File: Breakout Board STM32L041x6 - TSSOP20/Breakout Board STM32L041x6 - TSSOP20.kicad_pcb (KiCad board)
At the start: 2 copper layers, 35.6 x 33 mm, 35 parts, among them J1 Conn_01x10, J2 Conn_01x10, SW1 reset switch, SW2 ibm m, U1 STM32L041F6P7, Y1 Crystal 32768

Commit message: Update
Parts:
- removed ? (x4): , 
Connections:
- J1 pad 8: /key -> (no net)
- TP5 pad 1: Net-(TP5-Pad1) -> (no net)
- TP6 pad 1: Net-(TP6-Pad1) -> (no net)
- TP7 pad 1: Net-(TP7-Pad1) -> (no net)
- TP8 pad 1: Net-(TP8-Pad1) -> (no net)
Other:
- rule trace_min: 0.2 -> 0.25

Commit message: Update
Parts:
- added ?: , , F.Cu at (132.1, 76.2)
- added ?: , , F.Cu at (26.0, 0.00)
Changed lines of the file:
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@@
     (tracks 30)
     (zones 0)
-    (modules 31)
+    (modules 33)
     (nets 25)
   )
@@
     (add_net "Net-(R5-Pad2)")
   )
+  (module "" (layer F.Cu)
+    (at 132.08 76.2)
+    (fp_text reference "" (at 26.035 0) (layer F.SilkS)
+      (effects (font (size 1.27 1.27) (thickness 0.15)))
+    )
+    (fp_text value "" (at 26.035 0) (layer F.SilkS)
+      (effects (font (size 1.27 1.27) (thickness 0.15)))
+    )
+    (fp_text user vddext (at 9.525 6.985 -90) (layer B.SilkS)
+      (effects (font (size 0.8 0.8) (thickness 0.15)) (justify mirror))
+    )
+  )
+  (module "" (layer F.Cu)
+    (at 26.035 0)
+    (fp_text reference "" (at 135.995 73.13) (layer F.SilkS)
+      (effects (font (size 1.27 1.27) (thickness 0.15)))
+    )
+    (fp_text value "" (at 135.995 73.13) (layer F.SilkS)
+      (effects (font (size 1.27 1.27) (thickness 0.15)))
+    )
+    (fp_text user gnd (at 115.57 68.58 -90) (layer B.SilkS)
+      (effects (font (size 0.8 0.8) (thickness 0.15)) (justify mirror))
+    )
+    (fp_text user swclk (at 113.665 61.595) (layer B.SilkS)
+      (effects (font (size 0.8 0.8) (thickness 0.15)) (justify mirror))
+    )
+    (fp_text user swdio (at 115.57 65.405 -90) (layer B.SilkS)
+      (effects (font (size 0.8 0.8) (thickness 0.15)) (justify mirror))
+    )
+  )
   (module "Breakout Board STM32L041x6 - TSSOP20:Crystal 32768 Hz Citizen - CMR200T32.768KDZB-UT" (layer B.Cu)
     (at 135.995 73.13 180)
@@
       (effects (font (size 0.8 0.8) (thickness 0.15)))
     )
-    (fp_text value 100nF (at 2.775 0.446) (layer F.SilkS)
+    (fp_text value 100nF (at 2.565 0.446) (layer F.SilkS)
       (effects (font (size 0.8 0.8) (thickness 0.15)))
     )
@@
     (effects (font (size 0.7 0.7) (thickness 0.13)) (justify left mirror))
   )
-  (gr_text x2 (at 145.415 60.96) (layer F.SilkS)
+  (gr_text x2 (at 146.05 59.055) (layer F.SilkS)
     (effects (font (size 0.8 0.8) (thickness 0.15)))
   )
@@
     (effects (font (size 0.8 0.8) (thickness 0.15)) (justify mirror))
   )
-  (gr_text x2 (at 145.415 60.96) (layer B.SilkS)
+  (gr_text x2 (at 146.05 59.055) (layer B.SilkS)
     (effects (font (size 0.8 0.8) (thickness 0.15)) (justify mirror))
   )

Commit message: Update
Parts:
- SW1: value reset switch -> reset
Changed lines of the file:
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@@
       (effects (font (size 0.8 0.8) (thickness 0.15)))
     )
-    (fp_text value "reset switch" (at 4.05 9.85 180) (layer F.SilkS)
+    (fp_text value reset (at 4.05 7.83 180) (layer F.SilkS)
       (effects (font (size 0.8 0.8) (thickness 0.15)))
     )
@@
     (effects (font (size 0.7 0.7) (thickness 0.13)) (justify left mirror))
   )
-  (gr_text x2 (at 146.05 59.055) (layer F.SilkS)
+  (gr_text x2 (at 145.415 59.69) (layer F.SilkS)
     (effects (font (size 0.8 0.8) (thickness 0.15)))
   )
@@
     (effects (font (size 0.8 0.8) (thickness 0.15)) (justify mirror))
   )
-  (gr_text x2 (at 146.05 59.055) (layer B.SilkS)
+  (gr_text x2 (at 145.415 59.69) (layer B.SilkS)
     (effects (font (size 0.8 0.8) (thickness 0.15)) (justify mirror))
   )

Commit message: Update
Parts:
- removed ? (x2): , 
- SW1: value reset -> reset sw
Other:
- board text added: "swdio"
- board text added: "vddext"
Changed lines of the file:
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@@
   (general
     (thickness 1.6)
-    (drawings 92)
+    (drawings 95)
     (tracks 30)
     (zones 0)
-    (modules 33)
+    (modules 31)
     (nets 25)
   )
@@
     (add_net "Net-(R5-Pad2)")
   )
-  (module "" (layer F.Cu)
-    (at 132.08 76.2)
-    (fp_text reference "" (at 26.035 0) (layer F.SilkS)
-      (effects (font (size 1.27 1.27) (thickness 0.15)))
-    )
-    (fp_text value "" (at 26.035 0) (layer F.SilkS)
-      (effects (font (size 1.27 1.27) (thickness 0.15)))
-    )
-    (fp_text user vddext (at 9.525 6.985 -90) (layer B.SilkS)
-      (effects (font (size 0.8 0.8) (thickness 0.15)) (justify mirror))
-    )
-  )
-  (module "" (layer F.Cu)
-    (at 26.035 0)
-    (fp_text reference "" (at 135.995 73.13) (layer F.SilkS)
-      (effects (font (size 1.27 1.27) (thickness 0.15)))
-    )
-    (fp_text value "" (at 135.995 73.13) (layer F.SilkS)
-      (effects (font (size 1.27 1.27) (thickness 0.15)))
-    )
-    (fp_text user gnd (at 115.57 68.58 -90) (layer B.SilkS)
-      (effects (font (size 0.8 0.8) (thickness 0.15)) (justify mirror))
-    )
-    (fp_text user swclk (at 113.665 61.595) (layer B.SilkS)
-      (effects (font (size 0.8 0.8) (thickness 0.15)) (justify mirror))
-    )
-    (fp_text user swdio (at 115.57 65.405 -90) (layer B.SilkS)
-      (effects (font (size 0.8 0.8) (thickness 0.15)) (justify mirror))
-    )
-  )
   (module "Breakout Board STM32L041x6 - TSSOP20:Crystal 32768 Hz Citizen - CMR200T32.768KDZB-UT" (layer B.Cu)
     (at 135.995 73.13 180)
@@
       (effects (font (size 0.8 0.8) (thickness 0.15)))
     )
-    (fp_text value reset (at 4.05 7.83 180) (layer F.SilkS)
+    (fp_text value "reset sw" (at 4.05 8.846 180) (layer F.SilkS)
       (effects (font (size 0.8 0.8) (thickness 0.15)))
     )
@@
     (pad 1 thru_hole circle (at 0 0) (size 1.7 1.7) (drill 1) (layers *.Cu *.Mask))
   )
+  (gr_text vddext (at 141.605 83.185 90) (layer B.SilkS)
+    (effects (font (size 0.8 0.8) (thickness 0.15)) (justify mirror))
+  )
+  (gr_text gnd (at 141.605 68.58 90) (layer B.SilkS)
+    (effects (font (size 0.8 0.8) (thickness 0.15)) (justify mirror))
+  )
+  (gr_text swdio (at 141.605 65.405 90) (layer B.SilkS)
+    (effects (font (size 0.8 0.8) (thickness 0.15)) (justify mirror))
+  )
   (gr_text "ЕС1832\n17072019а0" (at 123.19 62.865 90) (layer F.SilkS)
     (effects (font (size 0.8 0.8) (thickness 0.15)))
@@
   (segment (start 124.42 70.63) (end 128.07 70.63) (width 0.25) (layer B.Cu) (net 2) (status 30))
   (segment (start 131.87 72.13) (end 132.12 71.88) (width 0.25) (layer B.Cu) (net 4) (status 30))
-  (via (at 130.192559 72.123691) (size 0.8) (drill 0.4) (layers F.Cu B.Cu) (net 4))
+  (via (at 130.192559 72.123691) (size 0.8) (drill 0.4) (layers F.Cu B.Cu) (net 4) (status 1000000))
   (segment (start 130.192559 72.632441) (end 130.192559 72.123691) (width 0.25) (layer F.Cu) (net 4))
   (segment (start 129.795 73.03) (end 130.192559 72.632441) (width 0.25) (layer F.Cu) (net 4))

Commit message: Update
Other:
- board text added: "!!! CHECK !!! NO 12.5 pF XTAL ALLOWED"
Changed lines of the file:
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@@
   (general
     (thickness 1.6)
-    (drawings 95)
+    (drawings 96)
     (tracks 30)
     (zones 0)
@@
   (page A4)
   (layers
-    (0 F.Cu signal)
-    (31 B.Cu signal)
+    (0 F.Cu signal hide)
+    (31 B.Cu signal hide)
     (32 B.Adhes user)
     (33 F.Adhes user)
@@
     (solder_mask_min_width 0.25)
     (aux_axis_origin 0 0)
-    (visible_elements 7FFFF7FF)
+    (visible_elements 7FFF77FF)
     (pcbplotparams
       (layerselection 0x010fc_ffffffff)
@@
     (pad 1 thru_hole circle (at 0 0) (size 1.7 1.7) (drill 1) (layers *.Cu *.Mask))
   )
+  (gr_text "!!! CHECK !!!\nNO 12.5 pF\nXTAL ALLOWED" (at 135.89 72.39) (layer B.SilkS)
+    (effects (font (size 0.5 0.5) (thickness 0.1)) (justify mirror))
+  )
   (gr_text vddext (at 141.605 83.185 90) (layer B.SilkS)

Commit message: Update
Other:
- board text added: "swclk"
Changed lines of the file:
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@@
   (general
     (thickness 1.6)
-    (drawings 96)
+    (drawings 97)
     (tracks 30)
     (zones 0)
@@
   (page A4)
   (layers
-    (0 F.Cu signal hide)
-    (31 B.Cu signal hide)
+    (0 F.Cu signal)
+    (31 B.Cu signal)
     (32 B.Adhes user)
     (33 F.Adhes user)
@@
     (solder_mask_min_width 0.25)
     (aux_axis_origin 0 0)
-    (visible_elements 7FFF77FF)
+    (visible_elements 7FFFF7FF)
     (pcbplotparams
       (layerselection 0x010fc_ffffffff)
@@
     (pad 1 thru_hole circle (at 0 0) (size 1.7 1.7) (drill 1) (layers *.Cu *.Mask))
   )
+  (gr_text swclk (at 139.7 61.595) (layer B.SilkS)
+    (effects (font (size 0.8 0.8) (thickness 0.15)))
+  )
   (gr_text "!!! CHECK !!!\nNO 12.5 pF\nXTAL ALLOWED" (at 135.89 72.39) (layer B.SilkS)

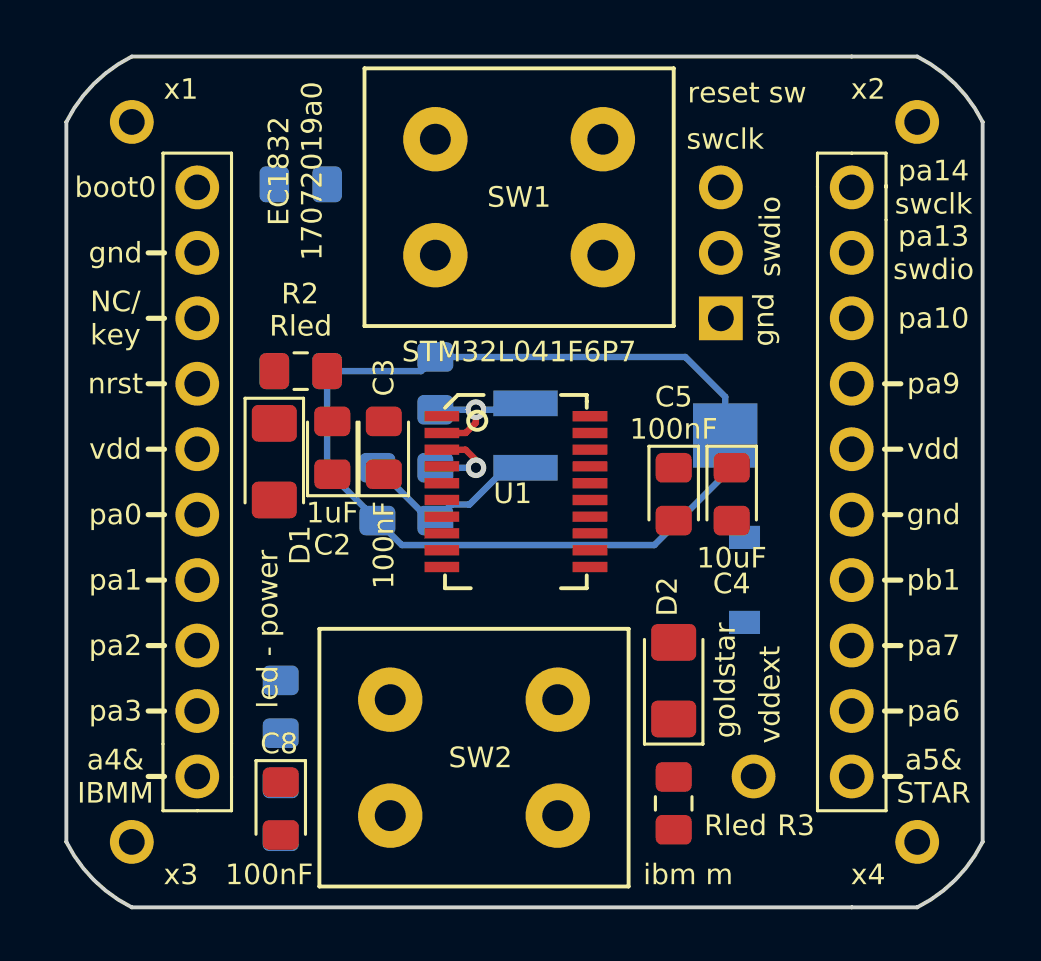
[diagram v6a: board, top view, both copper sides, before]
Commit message: Update - DRC check drill sizes - whatever, for this board
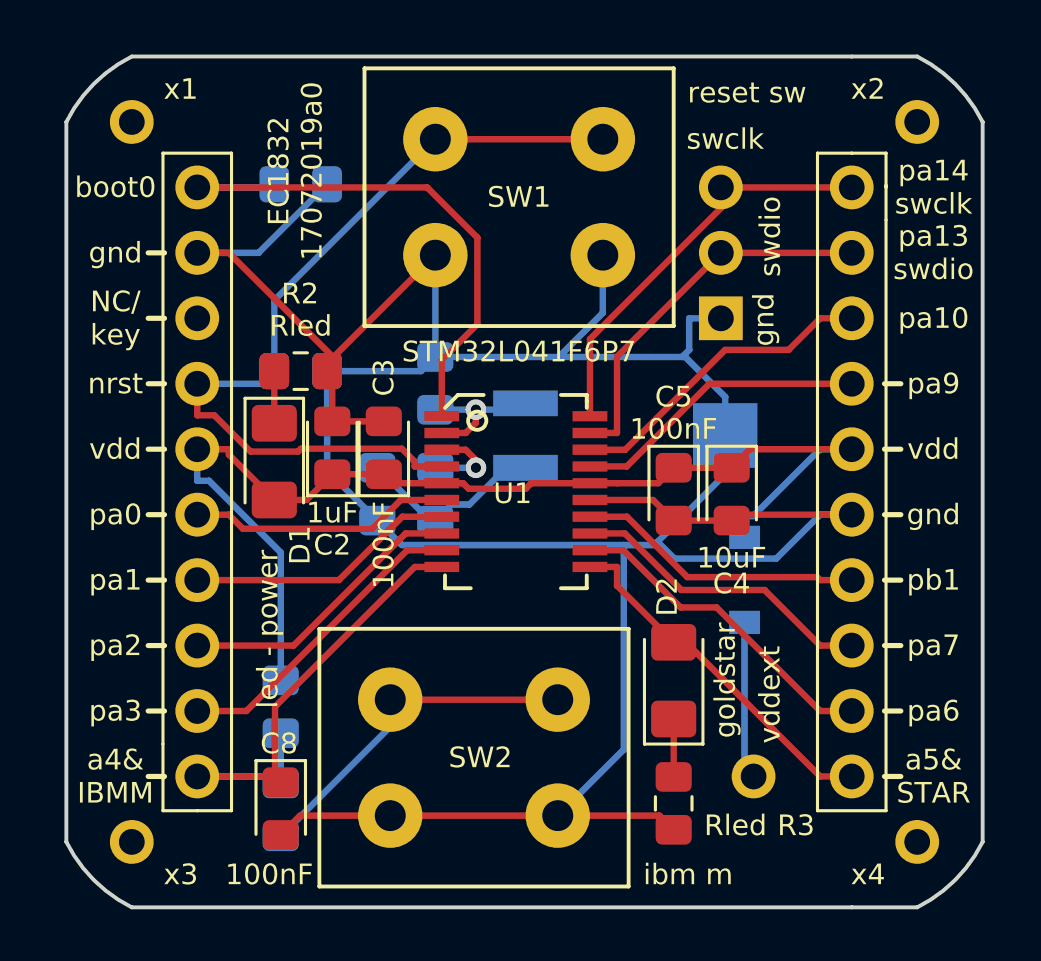
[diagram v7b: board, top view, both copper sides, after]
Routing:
- net GND: track 41.0 -> 122.2 mm
- net /vdd: track 0.00 -> 44.3 mm
- net /nrst: track 0.00 -> 33.0 mm
- net /boot: track 0.00 -> 22.2 mm
- net /ibm-m: track 0.00 -> 19.9 mm
- net /swclk: track 0.00 -> 16.1 mm
- net /swdio: track 0.00 -> 14.8 mm
- net /goldstar: track 0.00 -> 14.0 mm
- net Net-(R5-Pad2): track 0.00 -> 13.6 mm
- net /pa6: track 0.00 -> 12.7 mm
- net /pa10: track 0.00 -> 12.3 mm
- net /pa3: track 0.00 -> 12.1 mm
- net /pa7: track 0.00 -> 12.0 mm
- net /pa9: track 0.00 -> 11.5 mm
- net /pa2: track 0.00 -> 11.3 mm
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
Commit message: Update
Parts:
- D2: value goldstar -> LED
- SW1: value reset sw -> reset switch
- SW2: value ibm m -> switch
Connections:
- net /goldstar renamed /led
- net /ibm-m renamed /switch
- J1 pad 8: (no net) -> /key
- TP5 pad 1: (no net) -> Net-(TP5-Pad1)
- TP6 pad 1: (no net) -> Net-(TP6-Pad1)
- TP7 pad 1: (no net) -> Net-(TP7-Pad1)
- TP8 pad 1: (no net) -> Net-(TP8-Pad1)
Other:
- board text added: "ATTENTION!!! NO 12.5 pF XTAL ALLOWED"
- board text added: "a4& switch"
- board text added: "a5& LED"
- board text added: "ЕС1832 18072019а0"
- board text added: "ЕС1832 Терминален възел 18072019а0"
- board text removed: "!!! CHECK !!! NO 12.5 pF XTAL ALLOWED"
- board text removed: "a4& IBMM"
- board text removed: "a5& STAR"
- board text removed: "ЕС1832 17072019а0"
- board text removed: "ЕС1832 Терминален възел (ъгъл) Проектирано и изработено в Република България"
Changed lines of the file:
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@@
     (zones 0)
     (modules 31)
-    (nets 25)
+    (nets 30)
   )
   (page A4)
@@
   (net 21 /pa9)
   (net 22 /pa10)
-  (net 23 /ibm-m)
-  (net 24 /goldstar)
+  (net 23 /switch)
+  (net 24 /led)
+  (net 25 /key)
+  (net 26 "Net-(TP5-Pad1)")
+  (net 27 "Net-(TP6-Pad1)")
+  (net 28 "Net-(TP7-Pad1)")
+  (net 29 "Net-(TP8-Pad1)")
   (net_class Default "This is the default net class."
     (clearance 0.25)
@@
     (diff_pair_width 0.4)
     (add_net /boot)
-    (add_net /goldstar)
-    (add_net /ibm-m)
+    (add_net /key)
+    (add_net /led)
     (add_net /nrst)
     (add_net /osc32in)
@@
     (add_net /swclk)
     (add_net /swdio)
+    (add_net /switch)
     (add_net /vdd)
     (add_net /vddext)
@@
     (add_net "Net-(D2-Pad1)")
     (add_net "Net-(R5-Pad2)")
+    (add_net "Net-(TP5-Pad1)")
+    (add_net "Net-(TP6-Pad1)")
+    (add_net "Net-(TP7-Pad1)")
+    (add_net "Net-(TP8-Pad1)")
   )
   (module "Breakout Board STM32L041x6 - TSSOP20:Crystal 32768 Hz Citizen - CMR200T32.768KDZB-UT" (layer B.Cu)
@@
       (effects (font (size 0.8 0.8) (thickness 0.15)))
     )
-    (fp_text value goldstar (at 0.0125 2 90) (layer F.SilkS)
+    (fp_text value LED (at 0.0125 2 90) (layer F.SilkS)
       (effects (font (size 0.8 0.8) (thickness 0.15)))
     )
@@
       (net 7 "Net-(D2-Pad1)"))
     (pad 2 smd roundrect (at 1.4875 0 90) (size 1.425 1.75) (layers F.Cu F.Paste F.Mask) (roundrect_rratio 0.175439)
-      (net 24 /goldstar))
+      (net 24 /led))
     (model ${KISYS3DMOD}/LED_SMD.3dshapes/LED_1206_3216Metric.wrl
       (at (xyz 0 0 0))
@@
     (tags "resistor handsolder")
     (attr smd)
-    (fp_text reference R4 (at 1.43 -5.365) (layer B.SilkS)
-      (effects (font (size 0.8 0.8) (thickness 0.15)) (justify mirror))
-    )
-    (fp_text value Rxtal (at 1.43 -2.825) (layer B.SilkS)
+    (fp_text reference R4 (at 1.43 -9.865) (layer B.SilkS)
+      (effects (font (size 0.8 0.8) (thickness 0.15)) (justify mirror))
+    )
+    (fp_text value Rxtal (at 1.43 -7.325) (layer B.SilkS)
       (effects (font (size 0.8 0.8) (thickness 0.15)) (justify mirror))
     )
@@
       (effects (font (size 0.8 0.8) (thickness 0.15)))
     )
-    (fp_text value "reset sw" (at 4.05 8.846 180) (layer F.SilkS)
+    (fp_text value "reset switch" (at 3.38 9.88 180) (layer F.SilkS)
       (effects (font (size 0.8 0.8) (thickness 0.15)))
     )
@@
       (net 16 /pa1))
     (pad 10 smd rect (at 2.925 2.875 270) (size 0.4 1.35) (layers F.Cu F.Paste F.Mask)
-      (net 23 /ibm-m))
+      (net 23 /switch))
     (pad 9 smd rect (at 2.275 2.875 270) (size 0.4 1.35) (layers F.Cu F.Paste F.Mask)
       (net 14 /pa3))
     (pad 11 smd rect (at 2.925 -2.875 270) (size 0.4 1.35) (layers F.Cu F.Paste F.Mask)
-      (net 24 /goldstar))
+      (net 24 /led))
     (pad 12 smd rect (at 2.275 -2.875 270) (size 0.4 1.35) (layers F.Cu F.Paste F.Mask)
       (net 18 /pa6))
@@
       (effects (font (size 0.8 0.8) (thickness 0.15)))
     )
-    (fp_text value "ibm m" (at -4.54 8.31 180) (layer F.SilkS)
+    (fp_text value switch (at -4.54 8.31 180) (layer F.SilkS)
       (effects (font (size 0.8 0.8) (thickness 0.15)))
     )
@@
     )
     (pad 1 smd roundrect (at -1.025 0 270) (size 1.15 1.4) (layers B.Cu B.Paste B.Mask) (roundrect_rratio 0.217391)
-      (net 23 /ibm-m))
+      (net 23 /switch))
     (pad 2 smd roundrect (at 1.025 0 270) (size 1.15 1.4) (layers B.Cu B.Paste B.Mask) (roundrect_rratio 0.217391)
       (net 13 "Net-(R5-Pad2)"))
@@
     )
     (pad 1 thru_hole circle (at 0 0 180) (size 1.7 1.7) (drill 1) (layers *.Cu *.Mask)
-      (net 23 /ibm-m))
+      (net 23 /switch))
     (pad 2 thru_hole oval (at 0 2.54 180) (size 1.7 1.7) (drill 1) (layers *.Cu *.Mask)
       (net 14 /pa3))
@@
     (pad 7 thru_hole oval (at 0 15.24 180) (size 1.7 1.7) (drill 1) (layers *.Cu *.Mask)
       (net 1 /nrst))
-    (pad 8 thru_hole oval (at 0 17.78 180) (size 1.7 1.7) (drill 1) (layers *.Cu *.Mask))
+    (pad 8 thru_hole oval (at 0 17.78 180) (size 1.7 1.7) (drill 1) (layers *.Cu *.Mask)
+      (net 25 /key))
     (pad 9 thru_hole oval (at 0 20.32 180) (size 1.7 1.7) (drill 1) (layers *.Cu *.Mask)
       (net 2 GND))
@@
     (fp_line (start -1.22 -1.27) (end 0.685 -1.27) (layer F.Fab) (width 0.1))
     (pad 10 thru_hole oval (at 0 22.86) (size 1.7 1.7) (drill 1) (layers *.Cu *.Mask)
-      (net 24 /goldstar))
+      (net 24 /led))
     (pad 9 thru_hole oval (at 0 20.32) (size 1.7 1.7) (drill 1) (layers *.Cu *.Mask)
       (net 18 /pa6))
@@
     )
     (pad 1 smd roundrect (at -1.025 0 270) (size 1.15 1.4) (layers F.Cu F.Paste F.Mask) (roundrect_rratio 0.217391)
-      (net 23 /ibm-m))
+      (net 23 /switch))
     (pad 2 smd roundrect (at 1.025 0 270) (size 1.15 1.4) (layers F.Cu F.Paste F.Mask) (roundrect_rratio 0.217391)
       (net 2 GND))
@@
       (net 3 /vdd))
     (pad 2 smd roundrect (at 1.025 0 270) (size 1.15 1.4) (layers B.Cu B.Paste B.Mask) (roundrect_rratio 0.217391)
-      (net 23 /ibm-m))
+      (net 23 /switch))
     (model ${KISYS3DMOD}/Resistor_SMD.3dshapes/R_0805_2012Metric.wrl
       (at (xyz 0 0 0))
@@
       (effects (font (size 1 1) (thickness 0.15)))
     )
-    (pad 1 thru_hole circle (at 0 0) (size 1.7 1.7) (drill 1) (layers *.Cu *.Mask))
+    (pad 1 thru_hole circle (at 0 0) (size 1.7 1.7) (drill 1) (layers *.Cu *.Mask)
+      (net 26 "Net-(TP5-Pad1)"))
   )
   (module "Breakout Board STM32L041x6 - TSSOP20:TestPoint 2.54mm round" (layer F.Cu)
@@
       (effects (font (size 1 1) (thickness 0.15)))
     )
-    (pad 1 thru_hole circle (at 0 0) (size 1.7 1.7) (drill 1) (layers *.Cu *.Mask))
+    (pad 1 thru_hole circle (at 0 0) (size 1.7 1.7) (drill 1) (layers *.Cu *.Mask)
+      (net 27 "Net-(TP6-Pad1)"))
   )
   (module "Breakout Board STM32L041x6 - TSSOP20:TestPoint 2.54mm round" (layer F.Cu)
@@
       (effects (font (size 1 1) (thickness 0.15)))
     )
-    (pad 1 thru_hole circle (at 0 0) (size 1.7 1.7) (drill 1) (layers *.Cu *.Mask))
+    (pad 1 thru_hole circle (at 0 0) (size 1.7 1.7) (drill 1) (layers *.Cu *.Mask)
+      (net 28 "Net-(TP7-Pad1)"))
   )
   (module "Breakout Board STM32L041x6 - TSSOP20:TestPoint 2.54mm round" (layer F.Cu)
@@
       (effects (font (size 1 1) (thickness 0.15)))
     )
-    (pad 1 thru_hole circle (at 0 0) (size 1.7 1.7) (drill 1) (layers *.Cu *.Mask))
+    (pad 1 thru_hole circle (at 0 0) (size 1.7 1.7) (drill 1) (layers *.Cu *.Mask)
+      (net 29 "Net-(TP8-Pad1)"))
   )
   (gr_text swclk (at 139.7 61.595) (layer B.SilkS)
     (effects (font (size 0.8 0.8) (thickness 0.15)))
   )
-  (gr_text "!!! CHECK !!!\nNO 12.5 pF\nXTAL ALLOWED" (at 135.89 72.39) (layer B.SilkS)
+  (gr_text "ATTENTION!!!\nNO 12.5 pF\nXTAL ALLOWED" (at 135.89 72.39) (layer B.SilkS)
     (effects (font (size 0.5 0.5) (thickness 0.1)) (justify mirror))
   )
-  (gr_text vddext (at 141.605 83.185 90) (layer B.SilkS)
+  (gr_text vddext (at 139.25 86.25 90) (layer B.SilkS)
     (effects (font (size 0.8 0.8) (thickness 0.15)) (justify mirror))
   )
@@
     (effects (font (size 0.8 0.8) (thickness 0.15)) (justify mirror))
   )
-  (gr_text "ЕС1832\n17072019а0" (at 123.19 62.865 90) (layer F.SilkS)
-    (effects (font (size 0.8 0.8) (thickness 0.15)))
-  )
-  (gr_text "ЕС1832\nТерминален възел (ъгъл)\nПроектирано и изработено\nв Република България" (at 139.065 79.375) (layer B.SilkS)
-    (effects (font (size 0.7 0.7) (thickness 0.13)) (justify left mirror))
+  (gr_text "ЕС1832\n18072019а0" (at 123.19 62.865 90) (layer F.SilkS)
+    (effects (font (size 0.8 0.8) (thickness 0.15)))
+  )
+  (gr_text "ЕС1832\nТерминален възел\n18072019а0" (at 132.25 79.5) (layer B.SilkS)
+    (effects (font (size 0.7 0.7) (thickness 0.13)) (justify mirror))
   )
   (gr_text x2 (at 145.415 59.69) (layer F.SilkS)
@@
     (effects (font (size 0.8 0.8) (thickness 0.15)) (justify mirror))
   )
-  (gr_text "a4&\nIBMM" (at 116.205 86.36) (layer B.SilkS)
+  (gr_text "a4&\nswitch" (at 116.205 86.36) (layer B.SilkS)
     (effects (font (size 0.8 0.8) (thickness 0.15)) (justify mirror))
   )
@@
     (effects (font (size 0.8 0.8) (thickness 0.15)) (justify mirror))
   )
-  (gr_text "a5&\nSTAR" (at 147.955 86.36) (layer B.SilkS)
+  (gr_text "a5&\nLED" (at 147.955 86.36) (layer B.SilkS)
     (effects (font (size 0.8 0.8) (thickness 0.15)) (justify mirror))
   )
@@
     (effects (font (size 0.8 0.8) (thickness 0.15)))
   )
-  (gr_text "a5&\nSTAR" (at 147.955 86.36) (layer F.SilkS)
-    (effects (font (size 0.8 0.8) (thickness 0.15)))
-  )
-  (gr_text "a4&\nIBMM" (at 116.205 86.36) (layer F.SilkS)
-    (effects (font (size 0.8 0.8) (thickness 0.15)))
-  )
+  (gr_text "a5&\nLED" (at 147.955 86.36) (layer F.SilkS)
+    (effects (font (size 0.8 0.8) (thickness 0.15)))
+  )
+  (gr_text "a4&\nswitch" (at 116.205 86.36) (layer F.SilkS)
+    (effects (font (size 0.8 0.8) (thickness 0.15)))
+  )
